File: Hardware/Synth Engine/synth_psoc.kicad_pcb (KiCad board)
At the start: 2 copper layers, 124.5 x 129.5 mm, 229 parts, among them J1 Barrel_Jack, J10 Conn_01x13, J11 Conn_01x13, J13 Conn_01x05, J14 Conn_01x05, J15 Conn_01x05, J16 Conn_01x05, J2 Audio-Jack-2_Switch, J3 SWD_programming, J4 Conn_01x08, J5 Conn_01x08, J6 Conn_01x03, J7 Capsense_buttons, J8 Conn_01x13, J9 Conn_01x13, Q1 MMBT3904-TP, Q2 MMBT3904-TP, Q3 MMBT3904-TP, Q4 MMBT3904-TP, Q5 MMBFJ177, Q6 MMBFJ177, Q7 MMBFJ177, Q8 MMBFJ177, U1 TL074, U2 TL074, U3 TL074, U4 TL074, U5 TL074, U6 CY8C4246AZI-L445, U7 V7805-1000, U8 PT2399, Y1 Crystal

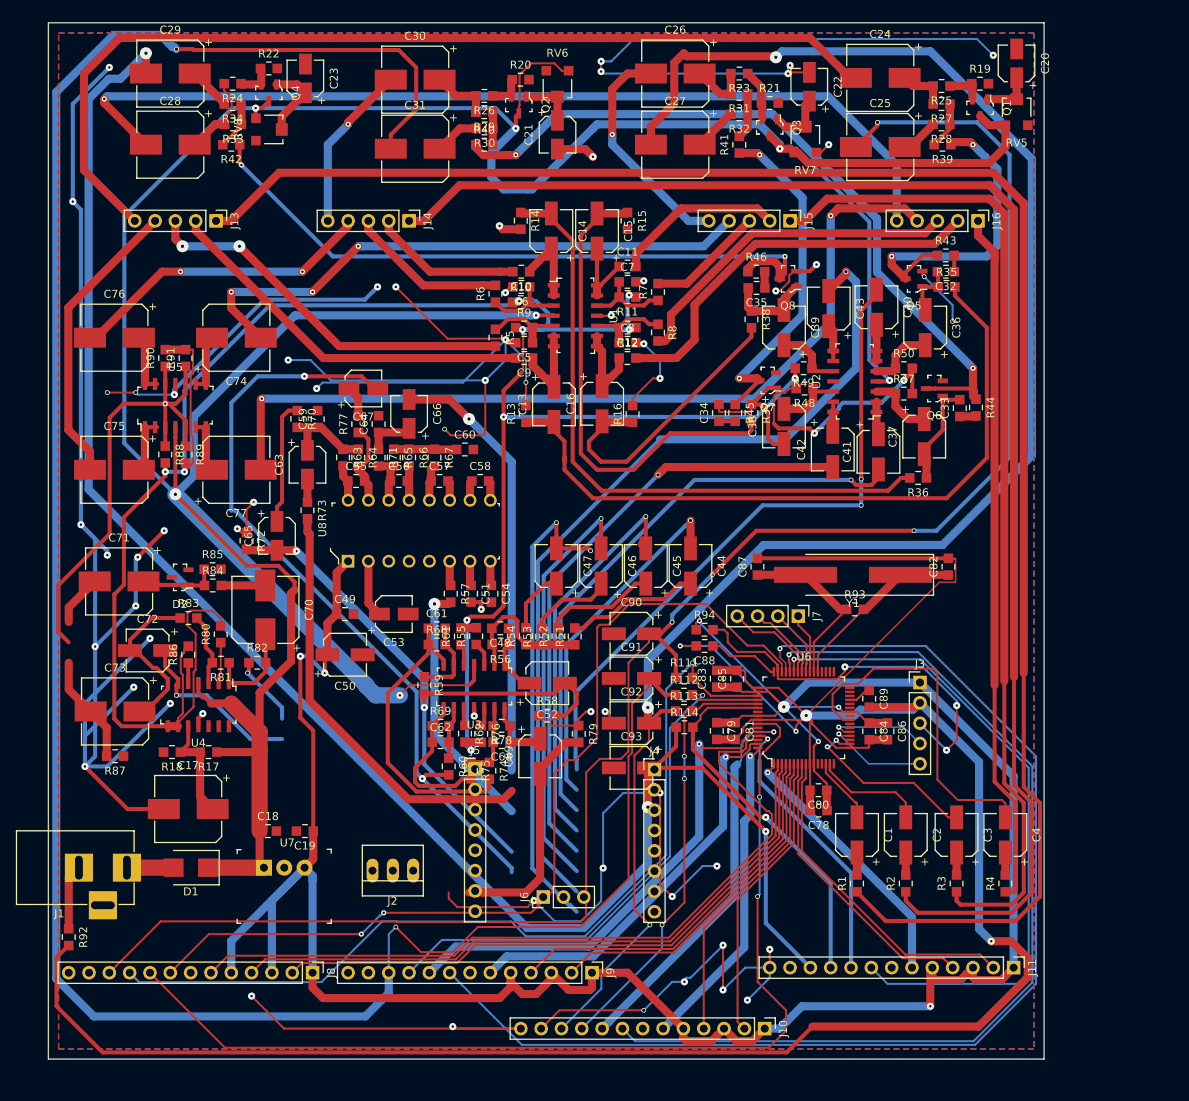
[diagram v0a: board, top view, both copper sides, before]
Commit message: redo connector routing with 2-row connectors
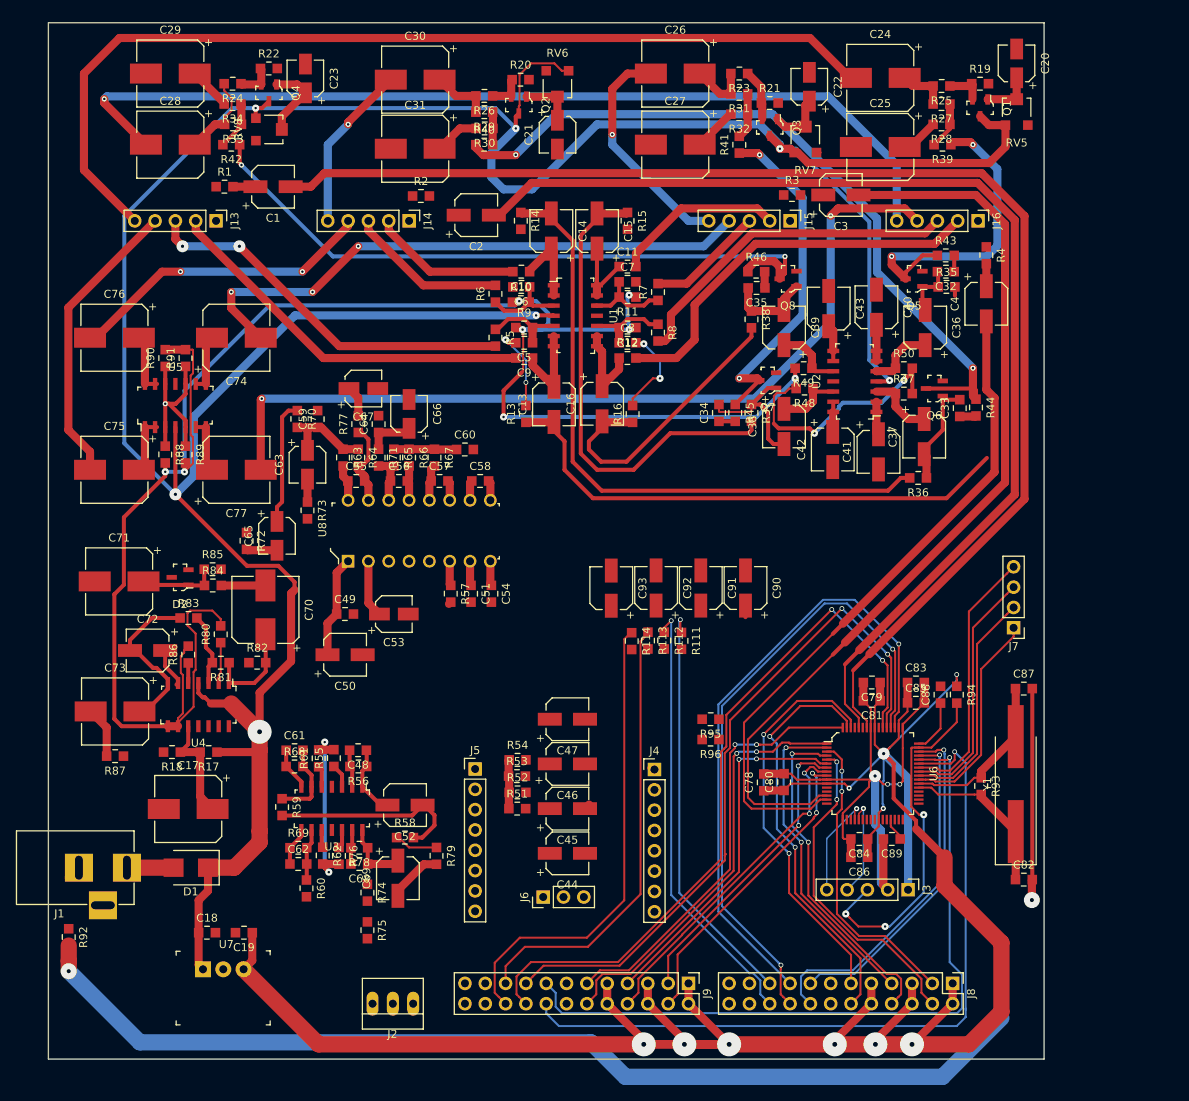
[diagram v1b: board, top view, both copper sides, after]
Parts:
- removed J10, J11: Conn_01x13, Pin_Headers:Pin_Header_Straight_1x13_Pitch2.54mm
- added R95: 0R, digikey-footprints:0805, F.Cu at (101.8, 109.2)
- added R96: 0R, digikey-footprints:0805, F.Cu at (101.8, 111.8)
- J8, J9: value Conn_01x13 -> Conn_02x12_Odd_Even; footprint Pin_Headers:Pin_Header_Straight_1x13_Pitch2.54mm -> Pin_Headers:Pin_Header_Straight_2x12_Pitch2.54mm
- moved R1 117.6 mm to (41.1, 42.7), turned to 0 degrees
- moved C1 109.1 mm to (47.1, 42.7), turned to 0 degrees
- moved R2 105.1 mm to (65.6, 43.8), turned to 0 degrees
- moved C2 94.3 mm to (72.5, 46.2), turned to 0 degrees
- moved R3 88.5 mm to (112.0, 43.7), turned to 0 degrees
- moved C3 81.3 mm to (118.1, 43.7), turned to 0 degrees
- moved J8 80.0 mm to (132.1, 142.2)
- moved R4 78.6 mm to (136.3, 51.2), turned to 270 degrees
- moved C4 66.4 mm to (136.3, 57.3), turned to 270 degrees
- moved C82 40.2 mm to (141.0, 129.3), turned to 0 degrees
- moved C44 39.1 mm to (83.9, 126.0), turned to 0 degrees
- moved C87 36.6 mm to (141.0, 105.4), turned to 0 degrees
- moved Y1 33.1 mm to (140.0, 117.3), turned to 90 degrees
- moved R94 32.6 mm to (132.6, 106.2), turned to 270 degrees
- moved C45 31.9 mm to (83.9, 120.4), turned to 0 degrees
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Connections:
- J8 pad 10: /Connectors/envelope_pwm_bypass_in_1 -> +5V
- J8 pad 11: /Microcontroller/envelope_pwm_1 -> /Connectors/osc1_speed
- J8 pad 12: GND -> /Connectors/osc2_speed
- J8 pad 13: GND -> /Connectors/osc1_hold
- J8 pad 2: /Connectors/osc1_freq_wiper -> +5V
- J8 pad 3: +5V -> /Connectors/osc1_freq_wiper
- J8 pad 4: /Connectors/osc1_pwm_wiper -> /Connectors/osc2_freq_wiper
- J8 pad 6: /Connectors/osc1_speed -> +5V
- J8 pad 7: /Connectors/osc1_hold -> /Connectors/osc1_pwm_wiper
- J8 pad 8: /Connectors/osc1_repeat -> /Connectors/osc2_pwm_wiper
- J8 pad 9: /Connectors/osc1_quant -> +5V
- J9 pad 10: /Connectors/envelope_pwm_bypass_in_2 -> +5V
- J9 pad 11: /Microcontroller/envelope_pwm_2 -> /Connectors/osc3_speed
- J9 pad 12: GND -> /Connectors/osc4_speed
- J9 pad 13: GND -> /Connectors/osc3_hold
- J9 pad 2: /Connectors/osc2_freq_wiper -> +5V
- J9 pad 3: +5V -> /Connectors/osc3_freq_wiper
- J9 pad 4: /Connectors/osc2_pwm_wiper -> /Connectors/osc4_freq_wiper
- J9 pad 6: /Connectors/osc2_speed -> +5V
- J9 pad 7: /Connectors/osc2_hold -> /Connectors/osc3_pwm_wiper
- J9 pad 8: /Connectors/osc2_repeat -> /Connectors/osc4_pwm_wiper
- J9 pad 9: /Connectors/osc2_quant -> +5V
- U6 pad 14: /Filters/osc1 -> /Filters/osc3
- U6 pad 15: /Filters/osc2 -> /Filters/osc4
- U6 pad 18: /Filters/osc3 -> Net-(U6-Pad18)
- U6 pad 22: Net-(U6-Pad22) -> /mcu_delay_in
- U6 pad 23: Net-(U6-Pad23) -> /mcu_delay_out
- U6 pad 24: /Filters/osc4 -> Net-(U6-Pad24)
- U6 pad 58: /Connectors/osc1_quant -> /Filters/osc1
- U6 pad 59: /Connectors/osc2_quant -> Net-(U6-Pad59)
- U6 pad 60: /Connectors/osc3_quant -> /Filters/osc2
- U6 pad 61: /Connectors/osc4_quant -> Net-(U6-Pad61)
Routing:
- net GND: track 614.0 -> 31.4 mm, vias 60 -> 4
- net /Microcontroller/envelope_pwm_2: track 289.7 -> 55.1 mm, vias 2 -> 1
- net /Connectors/freq_in_1: track 218.2 -> 0.06 mm
- net /Connectors/freq_in_2: track 183.5 -> 0.00 mm
- net /Microcontroller/envelope_pwm_1: track 224.9 -> 54.0 mm, vias 4 -> 1
- net /Filters/osc1: track 8.39 -> 168.9 mm
- net /Microcontroller/envelope_pwm_3: track 215.0 -> 56.1 mm, vias 3 -> 0
- net /Microcontroller/envelope_pwm_4: track 213.0 -> 59.0 mm, vias 3 -> 0
- net /Filters/osc2: track 13.9 -> 141.7 mm
- net /Connectors/osc1_quant: track 127.7 -> 0.00 mm, vias 2 -> 0
- net /Connectors/freq_in_3: track 124.9 -> 0.00 mm
- net Net-(C43-Pad2): track 108.9 -> 0.00 mm, vias 1 -> 0
- net /Connectors/osc2_repeat: track 149.9 -> 44.8 mm
- net /Mixer and Effects/delay_out: track 97.3 -> 0.50 mm, vias 2 -> 0
- net GNDD: track 328.6 -> 233.7 mm, vias 4 -> 5
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- removed copper zone on B.Cu, net GND
- removed copper zone on F.Cu, net GND

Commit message: mostly done rerouting main board. Still some ground returns to take care of.
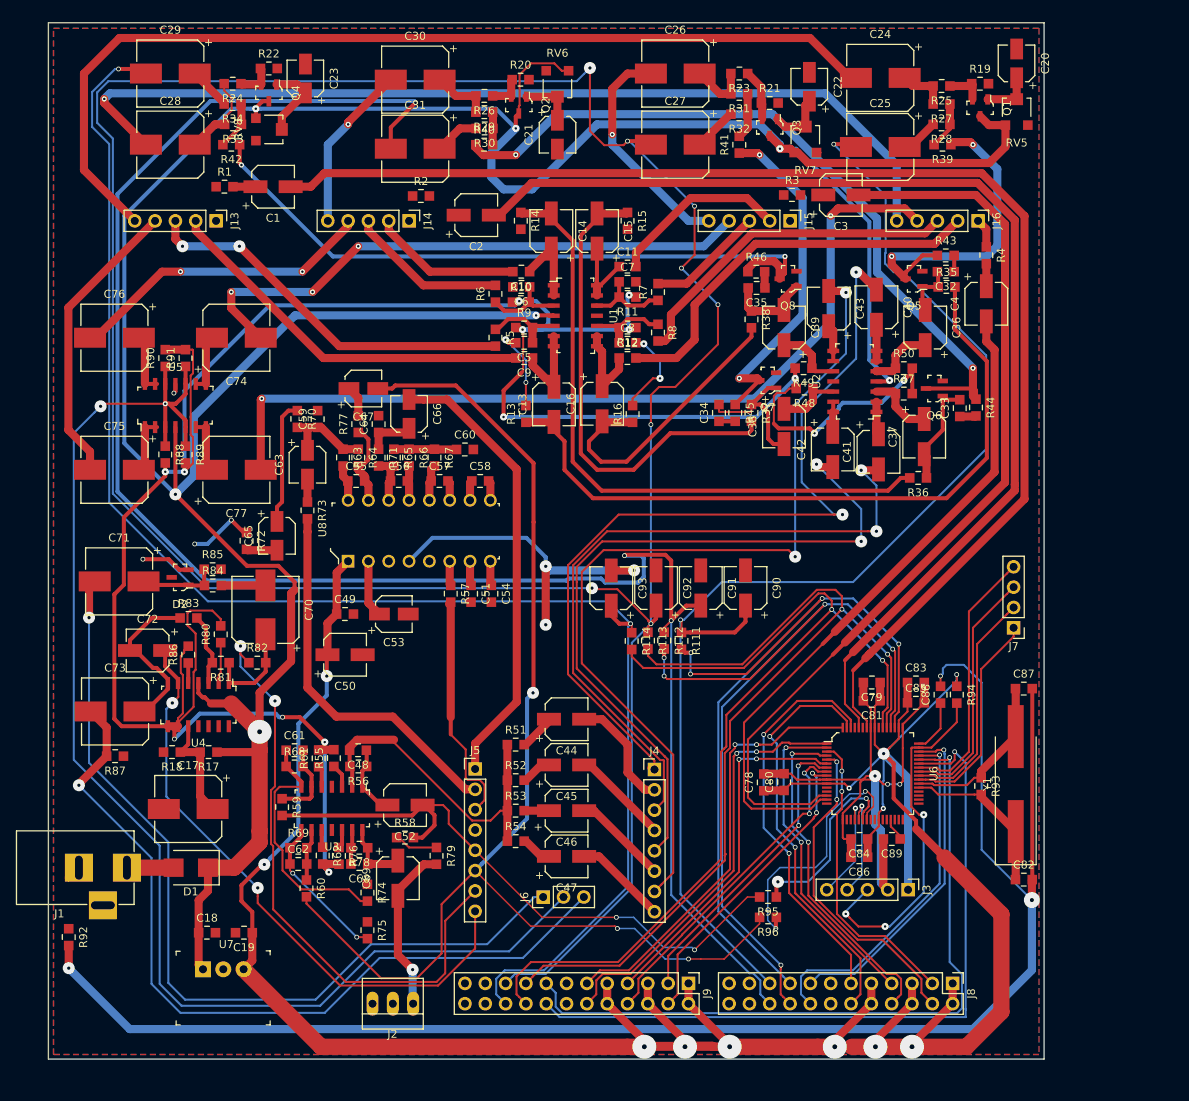
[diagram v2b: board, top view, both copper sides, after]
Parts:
- moved R96 23.4 mm to (109.0, 134.0)
- moved R95 23.4 mm to (109.0, 131.4)
- moved C47 17.1 mm to (83.8, 126.4)
- moved C44 16.8 mm to (83.8, 109.2)
- moved R54 10.2 mm to (77.5, 124.5)
- moved R51 8.00 mm to (77.5, 112.4)
- moved C46 5.84 mm to (83.8, 120.7)
- moved C45 5.46 mm to (83.8, 114.9)
- moved R53 4.32 mm to (77.5, 120.7)
- moved R52 1.54 mm to (77.5, 116.8)
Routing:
- net /Microcontroller/envelope_pwm_3: track 56.1 -> 334.6 mm, vias 0 -> 8
- net /Microcontroller/envelope_pwm_2: track 55.1 -> 235.6 mm, vias 1 -> 3
- net /Mixer and Effects/delay_out: track 0.50 -> 155.9 mm, vias 0 -> 3
- net /LFO Modulation and Routing/main_lfo: track 23.1 -> 166.6 mm, vias 1 -> 2
- net /Microcontroller/envelope_pwm_4: track 59.0 -> 195.0 mm, vias 0 -> 2
- net Net-(C43-Pad2): track 0.00 -> 111.7 mm, vias 0 -> 2
- net /LFO Modulation and Routing/lfo_square: track 0.00 -> 107.6 mm, vias 0 -> 1
- net /Microcontroller/envelope_pwm_1: track 54.0 -> 161.1 mm, vias 1 -> 2
- net Net-(C40-Pad2): track 1.40 -> 107.6 mm, vias 0 -> 2
- net /LFO Modulation and Routing/lfo_tri: track 6.42 -> 102.3 mm, vias 0 -> 1
- net Net-(C42-Pad2): track 0.00 -> 92.0 mm, vias 0 -> 2
- net Net-(C41-Pad2): track 1.42 -> 87.7 mm, vias 0 -> 2
- net /lfo_freq_in: track 0.00 -> 75.1 mm, vias 0 -> 2
- net /lfo_freq_out: track 5.02 -> 75.6 mm, vias 0 -> 2
- net GND: track 31.4 -> 89.0 mm, vias 4 -> 11
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- added copper zone on B.Cu, net GND
- added copper zone on F.Cu, net GND

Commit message: add quantization again, fix connectors again, add mounting holes to main board
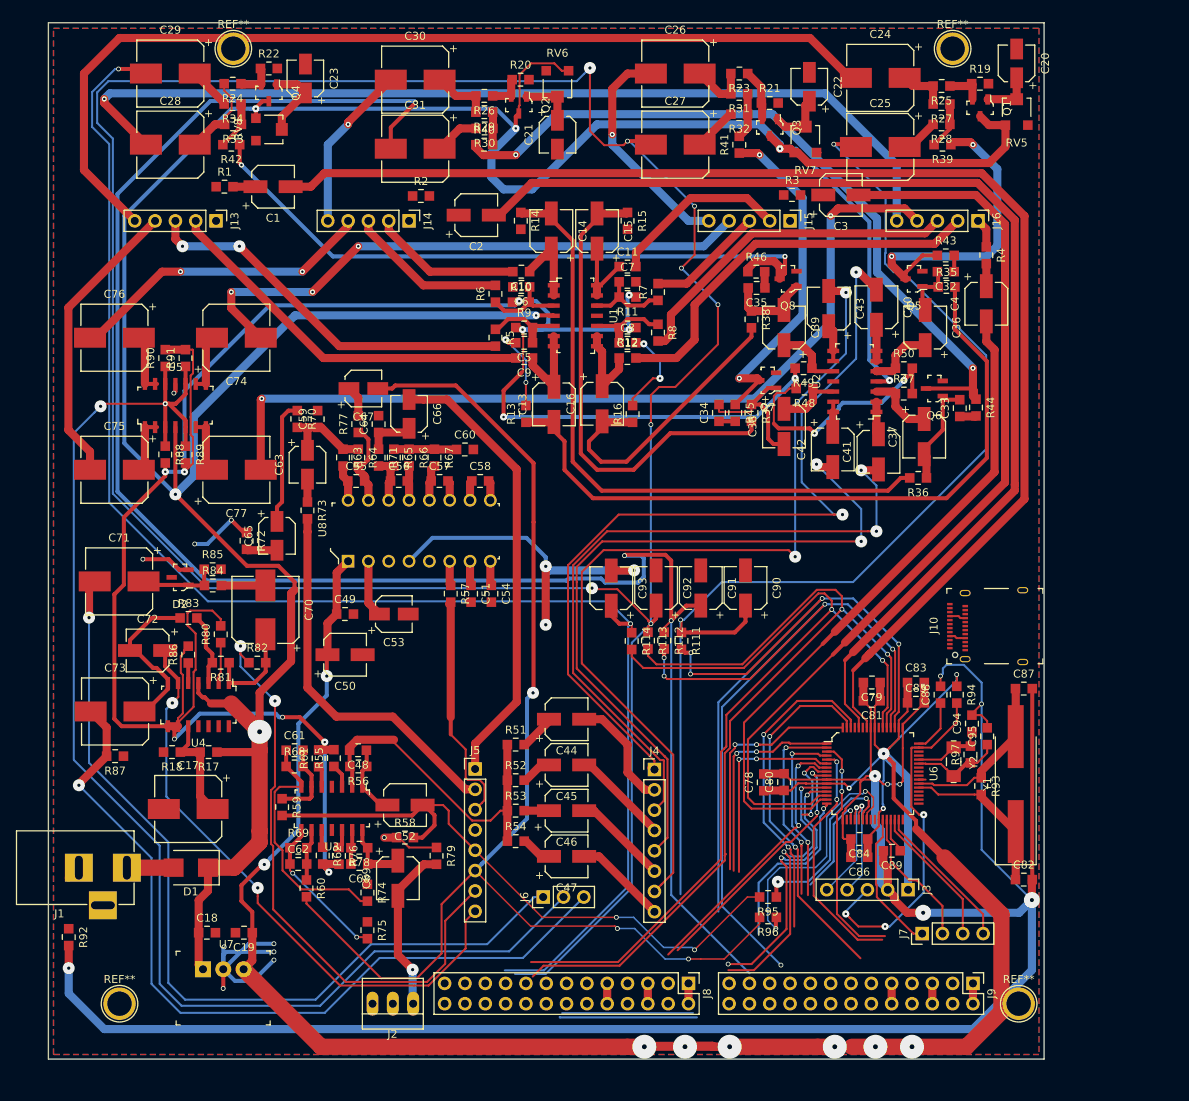
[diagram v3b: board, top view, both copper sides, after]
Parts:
- added C94: 22pF, digikey-footprints:0805, F.Cu at (134.5, 109.8)
- added C95: 22pF, digikey-footprints:0805, F.Cu at (136.4, 111.3)
- added J10: USB_C_Receptacle, digikey-footprints:USB_Type_C_Female__12401610E4_2A, F.Cu at (133.7, 97.6)
- added R97: 1MEG, digikey-footprints:0805, F.Cu at (134.3, 113.6)
- added REF**: 1pin, Connectors:1pin, F.Cu at (42.2, 25.4)
- added REF**: 1pin, Connectors:1pin, F.Cu at (132.1, 25.4)
- added REF**: 1pin, Connectors:1pin, F.Cu at (140.3, 144.8)
- added REF**: 1pin, Connectors:1pin, F.Cu at (27.9, 144.8)
- added Y2: 32.768kHz, digikey-footprints:1206, F.Cu at (132.2, 114.5)
- J8, J9: value Conn_02x12_Odd_Even -> Conn_02x13_Odd_Even; footprint Pin_Headers:Pin_Header_Straight_2x12_Pitch2.54mm -> Pin_Headers:Pin_Header_Straight_2x13_Pitch2.54mm
- Y1: value Crystal -> 16MHz
- moved J7 39.9 mm to (128.3, 136.0), turned to 90 degrees
- moved J9 35.6 mm to (134.6, 142.2)
- moved J8 33.0 mm to (99.1, 142.2)
- moved C89 1.48 mm to (124.5, 125.7)
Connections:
- J8 pad 11: /Connectors/osc1_speed -> /Connectors/osc3_speed
- J8 pad 12: /Connectors/osc2_speed -> /Connectors/osc4_speed
- J8 pad 13: /Connectors/osc1_hold -> /Connectors/osc3_quant
- J8 pad 14: /Connectors/osc2_hold -> /Connectors/osc4_quant
- J8 pad 15: /Connectors/osc1_repeat -> /Connectors/osc3_hold
- J8 pad 16: /Connectors/osc2_repeat -> /Connectors/osc4_hold
- J8 pad 17: /Connectors/envelope_pwm_bypass_in_1 -> /Connectors/osc3_repeat
- J8 pad 18: /Connectors/envelope_pwm_bypass_in_2 -> /Connectors/osc4_repeat
- J8 pad 19: /Microcontroller/envelope_pwm_1 -> /Connectors/envelope_pwm_bypass_in_3
- J8 pad 20: /Microcontroller/envelope_pwm_2 -> /Connectors/envelope_pwm_bypass_in_4
- J8 pad 21: GND -> /Microcontroller/envelope_pwm_3
- J8 pad 22: GND -> /Microcontroller/envelope_pwm_4
- J8 pad 3: /Connectors/osc1_freq_wiper -> /Connectors/osc3_freq_wiper
- J8 pad 4: /Connectors/osc2_freq_wiper -> /Connectors/osc4_freq_wiper
- J8 pad 7: /Connectors/osc1_pwm_wiper -> /Connectors/osc3_pwm_wiper
- J8 pad 8: /Connectors/osc2_pwm_wiper -> /Connectors/osc4_pwm_wiper
- J9 pad 11: /Connectors/osc3_speed -> /Connectors/osc1_speed
- J9 pad 12: /Connectors/osc4_speed -> /Connectors/osc2_speed
- J9 pad 13: /Connectors/osc3_hold -> /Connectors/osc1_quant
- J9 pad 14: /Connectors/osc4_hold -> /Connectors/osc2_quant
- J9 pad 15: /Connectors/osc3_repeat -> /Connectors/osc1_hold
- J9 pad 16: /Connectors/osc4_repeat -> /Connectors/osc2_hold
- J9 pad 17: /Connectors/envelope_pwm_bypass_in_3 -> /Connectors/osc1_repeat
- J9 pad 18: /Connectors/envelope_pwm_bypass_in_4 -> /Connectors/osc2_repeat
- J9 pad 19: /Microcontroller/envelope_pwm_3 -> /Connectors/envelope_pwm_bypass_in_1
- J9 pad 20: /Microcontroller/envelope_pwm_4 -> /Connectors/envelope_pwm_bypass_in_2
- J9 pad 21: GND -> /Microcontroller/envelope_pwm_1
- J9 pad 22: GND -> /Microcontroller/envelope_pwm_2
- J9 pad 3: /Connectors/osc3_freq_wiper -> /Connectors/osc1_freq_wiper
- J9 pad 4: /Connectors/osc4_freq_wiper -> /Connectors/osc2_freq_wiper
- J9 pad 7: /Connectors/osc3_pwm_wiper -> /Connectors/osc1_pwm_wiper
- J9 pad 8: /Connectors/osc4_pwm_wiper -> /Connectors/osc2_pwm_wiper
- U6 pad 12: Net-(U6-Pad12) -> /Connectors/osc4_repeat
- U6 pad 13: Net-(U6-Pad13) -> /Connectors/osc3_repeat
- U6 pad 16: Net-(U6-Pad16) -> /Connectors/osc2_repeat
- U6 pad 18: Net-(U6-Pad18) -> /mcu_delay_in
- U6 pad 19: Net-(U6-Pad19) -> /Connectors/osc1_repeat
- U6 pad 22: /mcu_delay_in -> /Connectors/osc4_quant
- U6 pad 23: /mcu_delay_out -> /Connectors/osc3_quant
- U6 pad 24: Net-(U6-Pad24) -> /Connectors/osc2_quant
- U6 pad 25: Net-(U6-Pad25) -> /Connectors/osc1_quant
- U6 pad 27: Net-(U6-Pad27) -> Net-(J7-Pad1)
- U6 pad 28: Net-(U6-Pad28) -> Net-(J7-Pad2)
- U6 pad 30: Net-(U6-Pad30) -> Net-(J7-Pad3)
- U6 pad 31: Net-(U6-Pad31) -> Net-(J7-Pad4)
- U6 pad 34: Net-(U6-Pad34) -> /Microcontroller/USB_D_p
- U6 pad 35: Net-(U6-Pad35) -> /Microcontroller/USB_D_n
- U6 pad 36: Net-(U6-Pad36) -> +5V
- U6 pad 39: Net-(J7-Pad1) -> Net-(U6-Pad39)
- U6 pad 40: Net-(J7-Pad2) -> Net-(U6-Pad40)
- U6 pad 41: Net-(J7-Pad3) -> /Microcontroller/osc4_hold
- U6 pad 42: Net-(J7-Pad4) -> /Microcontroller/osc3_hold
- U6 pad 43: /Connectors/osc4_repeat -> Net-(C95-Pad1)
- U6 pad 44: /Connectors/osc3_repeat -> Net-(C94-Pad1)
- U6 pad 45: /Connectors/osc2_repeat -> /Microcontroller/osc2_hold
- U6 pad 46: /Connectors/osc1_repeat -> /Microcontroller/osc1_hold
- U6 pad 55: Net-(U6-Pad55) -> /mcu_delay_out
- U6 pad 61: Net-(U6-Pad61) -> Net-(U6-Pad59)
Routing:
- net /Connectors/osc3_repeat: track 90.8 -> 33.5 mm, vias 1 -> 3
- net /Connectors/osc4_repeat: track 92.7 -> 35.6 mm, vias 1 -> 2
- net +5V: track 408.7 -> 368.8 mm
- net (no net): track 0.00 -> 33.6 mm
- net /Connectors/osc4_pwm_wiper: track 42.3 -> 10.1 mm
- net GND: track 89.0 -> 119.8 mm, vias 11 -> 17
- net /Connectors/osc1_repeat: track 41.9 -> 12.7 mm
- net /Connectors/osc4_speed: track 53.3 -> 27.0 mm
- net GNDD: track 282.3 -> 307.8 mm, vias 6 -> 8
- net /Connectors/osc3_speed: track 54.0 -> 30.2 mm
- net /Connectors/osc2_repeat: track 44.8 -> 21.9 mm
- net /Connectors/osc4_quant: track 0.00 -> 20.3 mm, vias 0 -> 1
- net /mcu_delay_in: track 23.4 -> 3.04 mm, vias 2 -> 1
- net /Connectors/osc3_pwm_wiper: track 45.0 -> 25.3 mm
- net /Connectors/osc2_pwm_wiper: track 42.5 -> 22.9 mm
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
